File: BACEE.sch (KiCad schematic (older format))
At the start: 12 parts

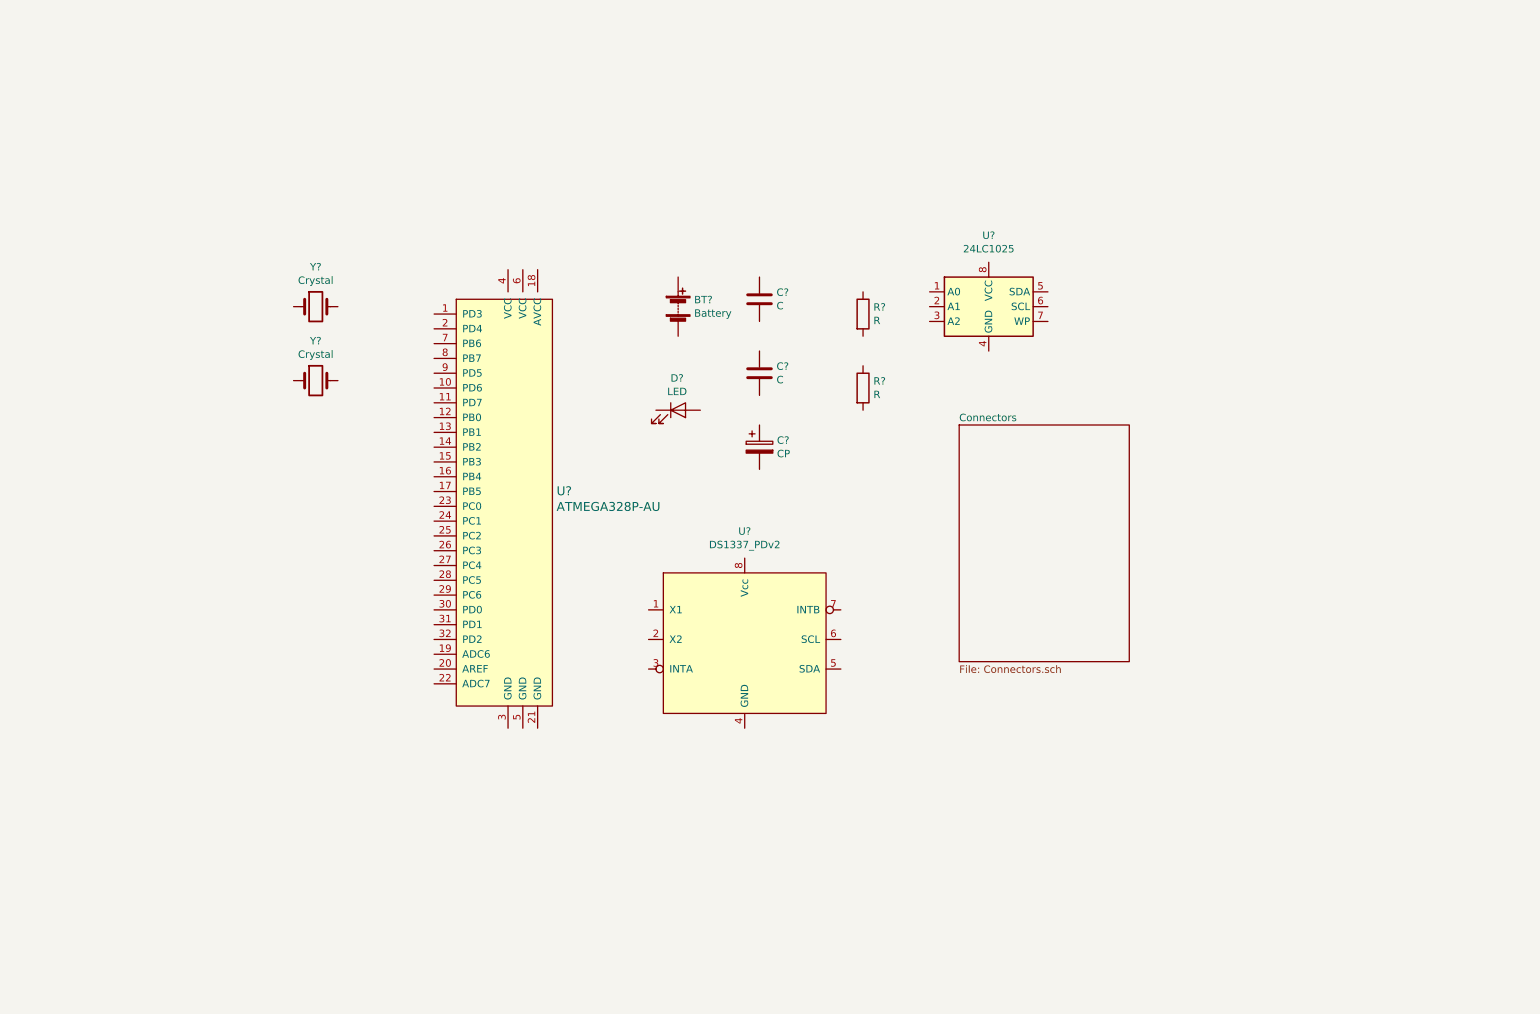
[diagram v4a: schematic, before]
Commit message: Arranged Symbols
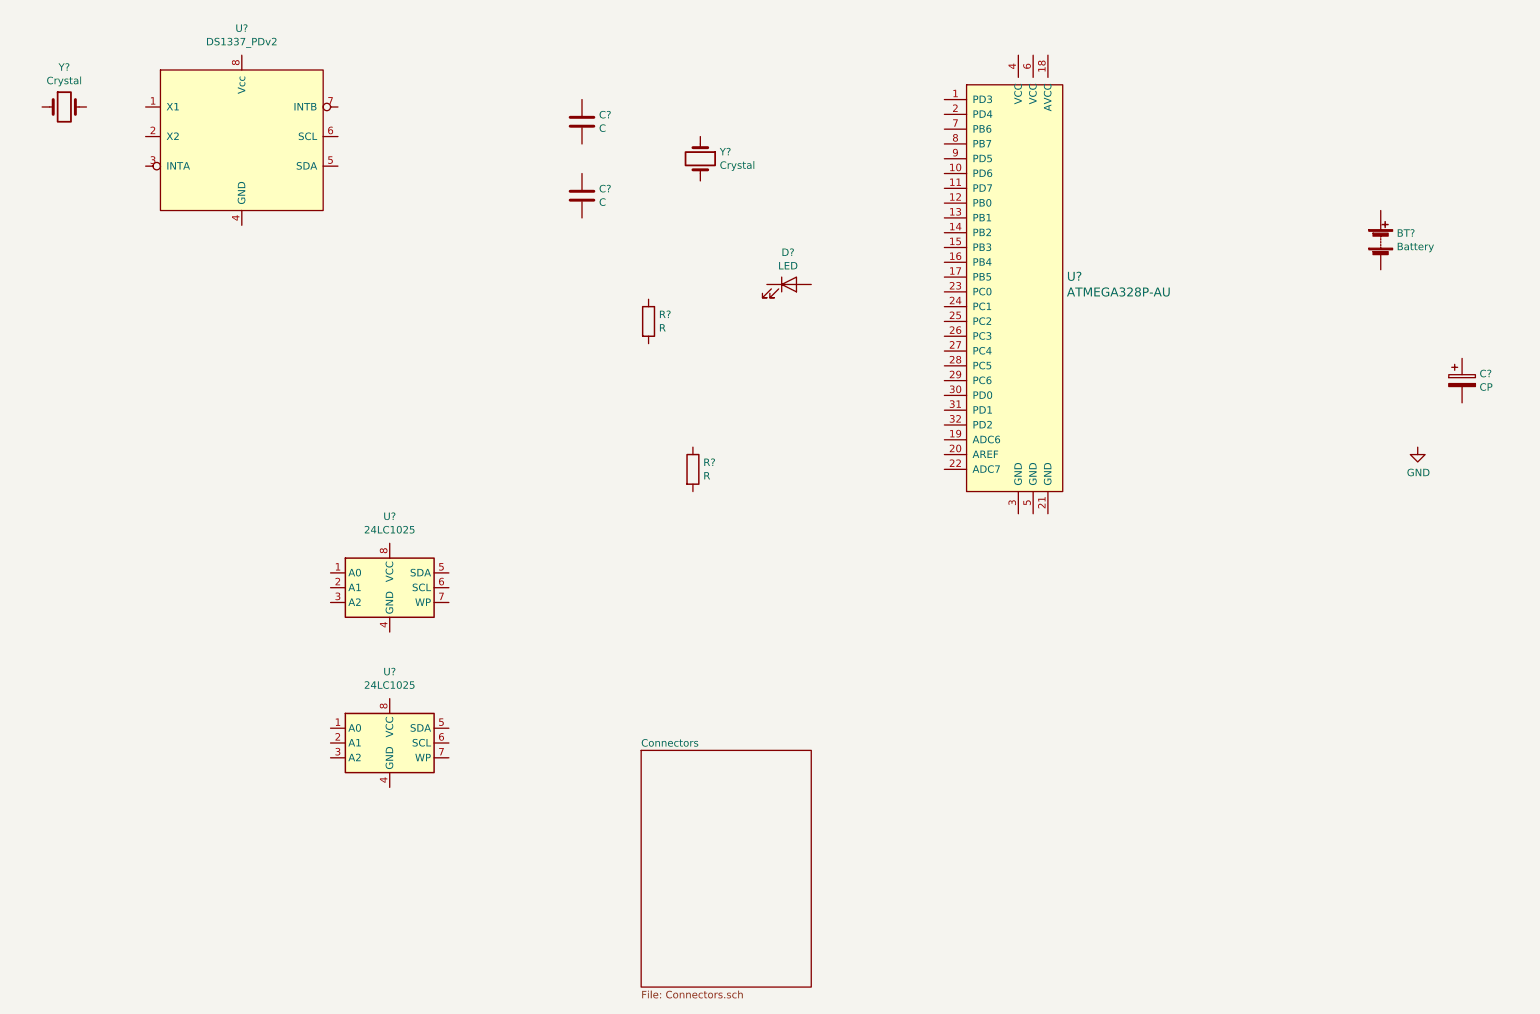
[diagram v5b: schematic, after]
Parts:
- added U?: 24LC1025, symbol Memory_EEPROM:24LC1025
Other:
- moved on the sheet: BT?, C?, D?, R?, U?, Y?
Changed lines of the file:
@@
 L Device:Battery BT?
 U 1 1 5EC0DCA7
-P 5050 3050
-F 0 "BT?" H 5158 3096 50  0000 L CNN
-F 1 "Battery" H 5158 3005 50  0000 L CNN
-F 2 "" V 5050 3110 50  0001 C CNN
-F 3 "~" V 5050 3110 50  0001 C CNN
-	1    5050 3050
+P 9800 2600
+F 0 "BT?" H 9908 2646 50  0000 L CNN
+F 1 "Battery" H 9908 2555 50  0000 L CNN
+F 2 "" V 9800 2660 50  0001 C CNN
+F 3 "~" V 9800 2660 50  0001 C CNN
+	1    9800 2600
 	1    0    0    -1
 $EndComp
@@
 L Device:C C?
 U 1 1 5EC0FEED
-P 5600 3000
-F 0 "C?" H 5715 3046 50  0000 L CNN
-F 1 "C" H 5715 2955 50  0000 L CNN
-F 2 "" H 5638 2850 50  0001 C CNN
-F 3 "~" H 5600 3000 50  0001 C CNN
-	1    5600 3000
+P 4400 1800
+F 0 "C?" H 4515 1846 50  0000 L CNN
+F 1 "C" H 4515 1755 50  0000 L CNN
+F 2 "" H 4438 1650 50  0001 C CNN
+F 3 "~" H 4400 1800 50  0001 C CNN
+	1    4400 1800
 	1    0    0    -1
 $EndComp
@@
 L Device:C C?
 U 1 1 5EC1064E
-P 5600 3500
-F 0 "C?" H 5715 3546 50  0000 L CNN
-F 1 "C" H 5715 3455 50  0000 L CNN
-F 2 "" H 5638 3350 50  0001 C CNN
-F 3 "~" H 5600 3500 50  0001 C CNN
-	1    5600 3500
+P 4400 2300
+F 0 "C?" H 4515 2346 50  0000 L CNN
+F 1 "C" H 4515 2255 50  0000 L CNN
+F 2 "" H 4438 2150 50  0001 C CNN
+F 3 "~" H 4400 2300 50  0001 C CNN
+	1    4400 2300
 	1    0    0    -1
 $EndComp
@@
 L Device:CP C?
 U 1 1 5EC10D42
-P 5600 4000
-F 0 "C?" H 5718 4046 50  0000 L CNN
-F 1 "CP" H 5718 3955 50  0000 L CNN
-F 2 "" H 5638 3850 50  0001 C CNN
-F 3 "~" H 5600 4000 50  0001 C CNN
-	1    5600 4000
+P 10350 3550
+F 0 "C?" H 10468 3596 50  0000 L CNN
+F 1 "CP" H 10468 3505 50  0000 L CNN
+F 2 "" H 10388 3400 50  0001 C CNN
+F 3 "~" H 10350 3550 50  0001 C CNN
+	1    10350 3550
 	1    0    0    -1
 $EndComp
@@
 L Device:LED D?
 U 1 1 5EC11BF2
-P 5050 3750
-F 0 "D?" H 5043 3966 50  0000 C CNN
-F 1 "LED" H 5043 3875 50  0000 C CNN
-F 2 "" H 5050 3750 50  0001 C CNN
-F 3 "~" H 5050 3750 50  0001 C CNN
-	1    5050 3750
+P 5800 2900
+F 0 "D?" H 5793 3116 50  0000 C CNN
+F 1 "LED" H 5793 3025 50  0000 C CNN
+F 2 "" H 5800 2900 50  0001 C CNN
+F 3 "~" H 5800 2900 50  0001 C CNN
+	1    5800 2900
 	1    0    0    -1
 $EndComp
@@
 L Device:R R?
 U 1 1 5EC1258B
-P 6300 3100
-F 0 "R?" H 6370 3146 50  0000 L CNN
-F 1 "R" H 6370 3055 50  0000 L CNN
-F 2 "" V 6230 3100 50  0001 C CNN
-F 3 "~" H 6300 3100 50  0001 C CNN
-	1    6300 3100
+P 4850 3150
+F 0 "R?" H 4920 3196 50  0000 L CNN
+F 1 "R" H 4920 3105 50  0000 L CNN
+F 2 "" V 4780 3150 50  0001 C CNN
+F 3 "~" H 4850 3150 50  0001 C CNN
+	1    4850 3150
 	1    0    0    -1
 $EndComp
@@
 L Device:R R?
 U 1 1 5EC1288A
-P 6300 3600
-F 0 "R?" H 6370 3646 50  0000 L CNN
-F 1 "R" H 6370 3555 50  0000 L CNN
-F 2 "" V 6230 3600 50  0001 C CNN
-F 3 "~" H 6300 3600 50  0001 C CNN
-	1    6300 3600
+P 5150 4150
+F 0 "R?" H 5220 4196 50  0000 L CNN
+F 1 "R" H 5220 4105 50  0000 L CNN
+F 2 "" V 5080 4150 50  0001 C CNN
+F 3 "~" H 5150 4150 50  0001 C CNN
+	1    5150 4150
 	1    0    0    -1
 $EndComp
@@
 L Memory_EEPROM:24LC1025 U?
 U 1 1 5EC12FEA
-P 7150 3050
-F 0 "U?" H 7150 3531 50  0000 C CNN
-F 1 "24LC1025" H 7150 3440 50  0000 C CNN
-F 2 "" H 7150 3050 50  0001 C CNN
-F 3 "http://ww1.microchip.com/downloads/en/DeviceDoc/21941B.pdf" H 7150 3050 50  0001 C CNN
-	1    7150 3050
+P 3100 4950
+F 0 "U?" H 3100 5431 50  0000 C CNN
+F 1 "24LC1025" H 3100 5340 50  0000 C CNN
+F 2 "" H 3100 4950 50  0001 C CNN
+F 3 "http://ww1.microchip.com/downloads/en/DeviceDoc/21941B.pdf" H 3100 4950 50  0001 C CNN
+	1    3100 4950
 	1    0    0    -1
 $EndComp
 $Sheet
-S 6950 3850 1150 1600
+S 4800 6050 1150 1600
 U 5EC178C4
 F0 "Connectors" 50
@@
 L dk_Embedded-Microcontrollers:ATMEGA328P-AU U?
 U 1 1 5EC1AF7B
-P 3900 4400
-F 0 "U?" H 4228 4503 60  0000 L CNN
-F 1 "ATMEGA328P-AU" H 4228 4397 60  0000 L CNN
-F 2 "digikey-footprints:TQFP-32_7x7mm" H 4100 4600 60  0001 L CNN
-F 3 "http://www.microchip.com/mymicrochip/filehandler.aspx?ddocname=en608326" H 4100 4700 60  0001 L CNN
-F 4 "ATMEGA328P-AU-ND" H 4100 4800 60  0001 L CNN "Digi-Key_PN"
-F 5 "ATMEGA328P-AU" H 4100 4900 60  0001 L CNN "MPN"
-F 6 "Integrated Circuits (ICs)" H 4100 5000 60  0001 L CNN "Category"
-F 7 "Embedded - Microcontrollers" H 4100 5100 60  0001 L CNN "Family"
-F 8 "http://www.microchip.com/mymicrochip/filehandler.aspx?ddocname=en608326" H 4100 5200 60  0001 L CNN "DK_Datasheet_Link"
-F 9 "/product-detail/en/microchip-technology/ATMEGA328P-AU/ATMEGA328P-AU-ND/1832260" H 4100 5300 60  0001 L CNN "DK_Detail_Page"
-F 10 "IC MCU 8BIT 32KB FLASH 32TQFP" H 4100 5400 60  0001 L CNN "Description"
-F 11 "Microchip Technology" H 4100 5500 60  0001 L CNN "Manufacturer"
-F 12 "Active" H 4100 5600 60  0001 L CNN "Status"
-	1    3900 4400
+P 7350 2950
+F 0 "U?" H 7678 3053 60  0000 L CNN
+F 1 "ATMEGA328P-AU" H 7678 2947 60  0000 L CNN
+F 2 "digikey-footprints:TQFP-32_7x7mm" H 7550 3150 60  0001 L CNN
+F 3 "http://www.microchip.com/mymicrochip/filehandler.aspx?ddocname=en608326" H 7550 3250 60  0001 L CNN
+F 4 "ATMEGA328P-AU-ND" H 7550 3350 60  0001 L CNN "Digi-Key_PN"
+F 5 "ATMEGA328P-AU" H 7550 3450 60  0001 L CNN "MPN"
+F 6 "Integrated Circuits (ICs)" H 7550 3550 60  0001 L CNN "Category"
+F 7 "Embedded - Microcontrollers" H 7550 3650 60  0001 L CNN "Family"
+F 8 "http://www.microchip.com/mymicrochip/filehandler.aspx?ddocname=en608326" H 7550 3750 60  0001 L CNN "DK_Datasheet_Link"
+F 9 "/product-detail/en/microchip-technology/ATMEGA328P-AU/ATMEGA328P-AU-ND/1832260" H 7550 3850 60  0001 L CNN "DK_Detail_Page"
+F 10 "IC MCU 8BIT 32KB FLASH 32TQFP" H 7550 3950 60  0001 L CNN "Description"
+F 11 "Microchip Technology" H 7550 4050 60  0001 L CNN "Manufacturer"
+F 12 "Active" H 7550 4150 60  0001 L CNN "Status"
+	1    7350 2950
 	1    0    0    -1
 $EndComp
@@
 L Arduino-Library:DS1337_PDv2 U?
 U 1 1 5EC1F02F
-P 5500 5300
-F 0 "U?" H 5500 6031 50  0000 C CNN
-F 1 "DS1337_PDv2" H 5500 5940 50  0000 C CNN
-F 2 "" H 6450 5800 50  0001 C CNN
-F 3 "https://4donline.ihs.com/images/VipMasterIC/IC/MAXM/MAXM-S-A0000633411/MAXM-S-A0000771822-1.pdf?hkey=52A5661711E402568146F3353EA87419" H 6450 5800 50  0001 C CNN
-	1    5500 5300
+P 2100 1900
+F 0 "U?" H 2100 2631 50  0000 C CNN
+F 1 "DS1337_PDv2" H 2100 2540 50  0000 C CNN
+F 2 "" H 3050 2400 50  0001 C CNN
+F 3 "https://4donline.ihs.com/images/VipMasterIC/IC/MAXM/MAXM-S-A0000633411/MAXM-S-A0000771822-1.pdf?hkey=52A5661711E402568146F3353EA87419" H 3050 2400 50  0001 C CNN
+	1    2100 1900
 	1    0    0    -1
 $EndComp
@@
 L Device:Crystal Y?
 U 1 1 5EC1F9D8
-P 2600 3050
-F 0 "Y?" H 2600 3318 50  0000 C CNN
-F 1 "Crystal" H 2600 3227 50  0000 C CNN
-F 2 "" H 2600 3050 50  0001 C CNN
-F 3 "~" H 2600 3050 50  0001 C CNN
-	1    2600 3050
+P 900 1700
+F 0 "Y?" H 900 1968 50  0000 C CNN
+F 1 "Crystal" H 900 1877 50  0000 C CNN
+F 2 "" H 900 1700 50  0001 C CNN
+F 3 "~" H 900 1700 50  0001 C CNN
+	1    900  1700
 	1    0    0    -1
 $EndComp
@@
 L Device:Crystal Y?
 U 1 1 5EC2101F
-P 2600 3550
-F 0 "Y?" H 2600 3818 50  0000 C CNN
-F 1 "Crystal" H 2600 3727 50  0000 C CNN
-F 2 "" H 2600 3550 50  0001 C CNN
-F 3 "~" H 2600 3550 50  0001 C CNN
-	1    2600 3550
+P 5200 2050
+F 0 "Y?" V 5154 2181 50  0000 L CNN
+F 1 "Crystal" V 5245 2181 50  0000 L CNN
+F 2 "" H 5200 2050 50  0001 C CNN
+F 3 "~" H 5200 2050 50  0001 C CNN
+	1    5200 2050
+	0    1    1    0
+$EndComp
+$Comp
+L Memory_EEPROM:24LC1025 U?
+U 1 1 5EC29420
+P 3100 6000
+F 0 "U?" H 3100 6481 50  0000 C CNN
+F 1 "24LC1025" H 3100 6390 50  0000 C CNN
+F 2 "" H 3100 6000 50  0001 C CNN
+F 3 "http://ww1.microchip.com/downloads/en/DeviceDoc/21941B.pdf" H 3100 6000 50  0001 C CNN
+	1    3100 6000
 	1    0    0    -1
 $EndComp
+$Comp
+L power:GND #PWR?
+U 1 1 5EC3997C
+P 10050 4000
+F 0 "#PWR?" H 10050 3750 50  0001 C CNN
+F 1 "GND" H 10055 3827 50  0000 C CNN
+F 2 "" H 10050 4000 50  0001 C CNN
+F 3 "" H 10050 4000 50  0001 C CNN
+	1    10050 4000
+	1    0    0    -1
+$EndComp
